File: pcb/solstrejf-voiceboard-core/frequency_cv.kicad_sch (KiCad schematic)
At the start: 23 parts, among them U5 LM324, U7 L78L12, U8 L79L12

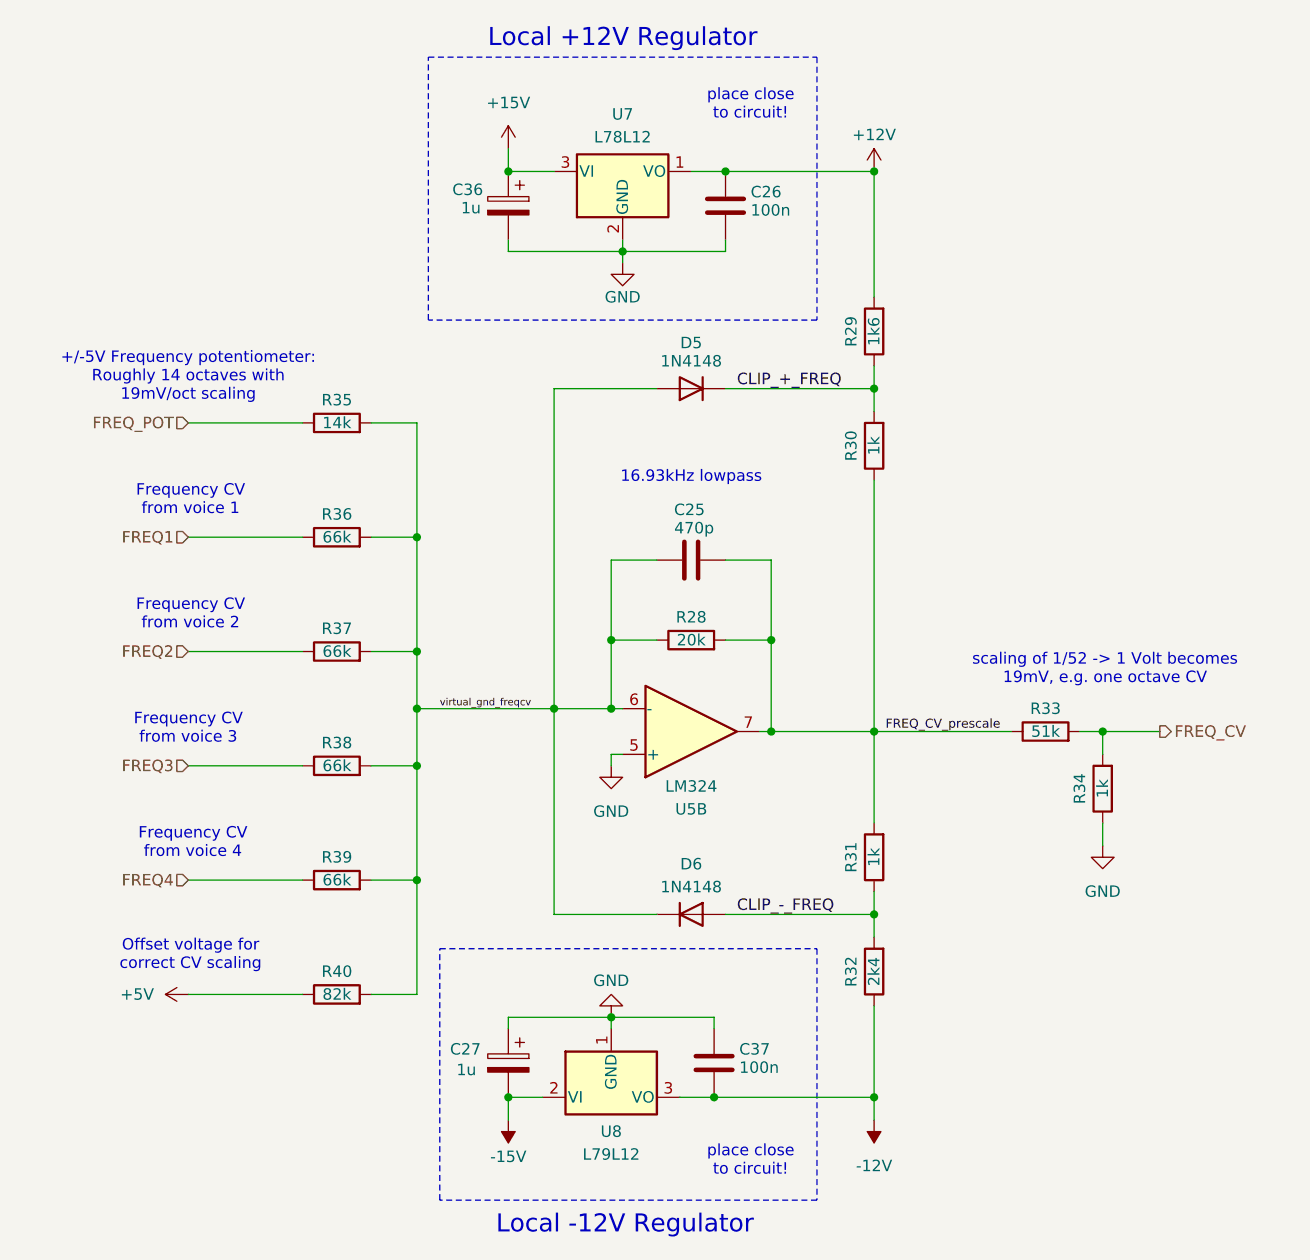
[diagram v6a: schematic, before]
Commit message: Updated values of electrolytic caps on voice board to match in the ibom.
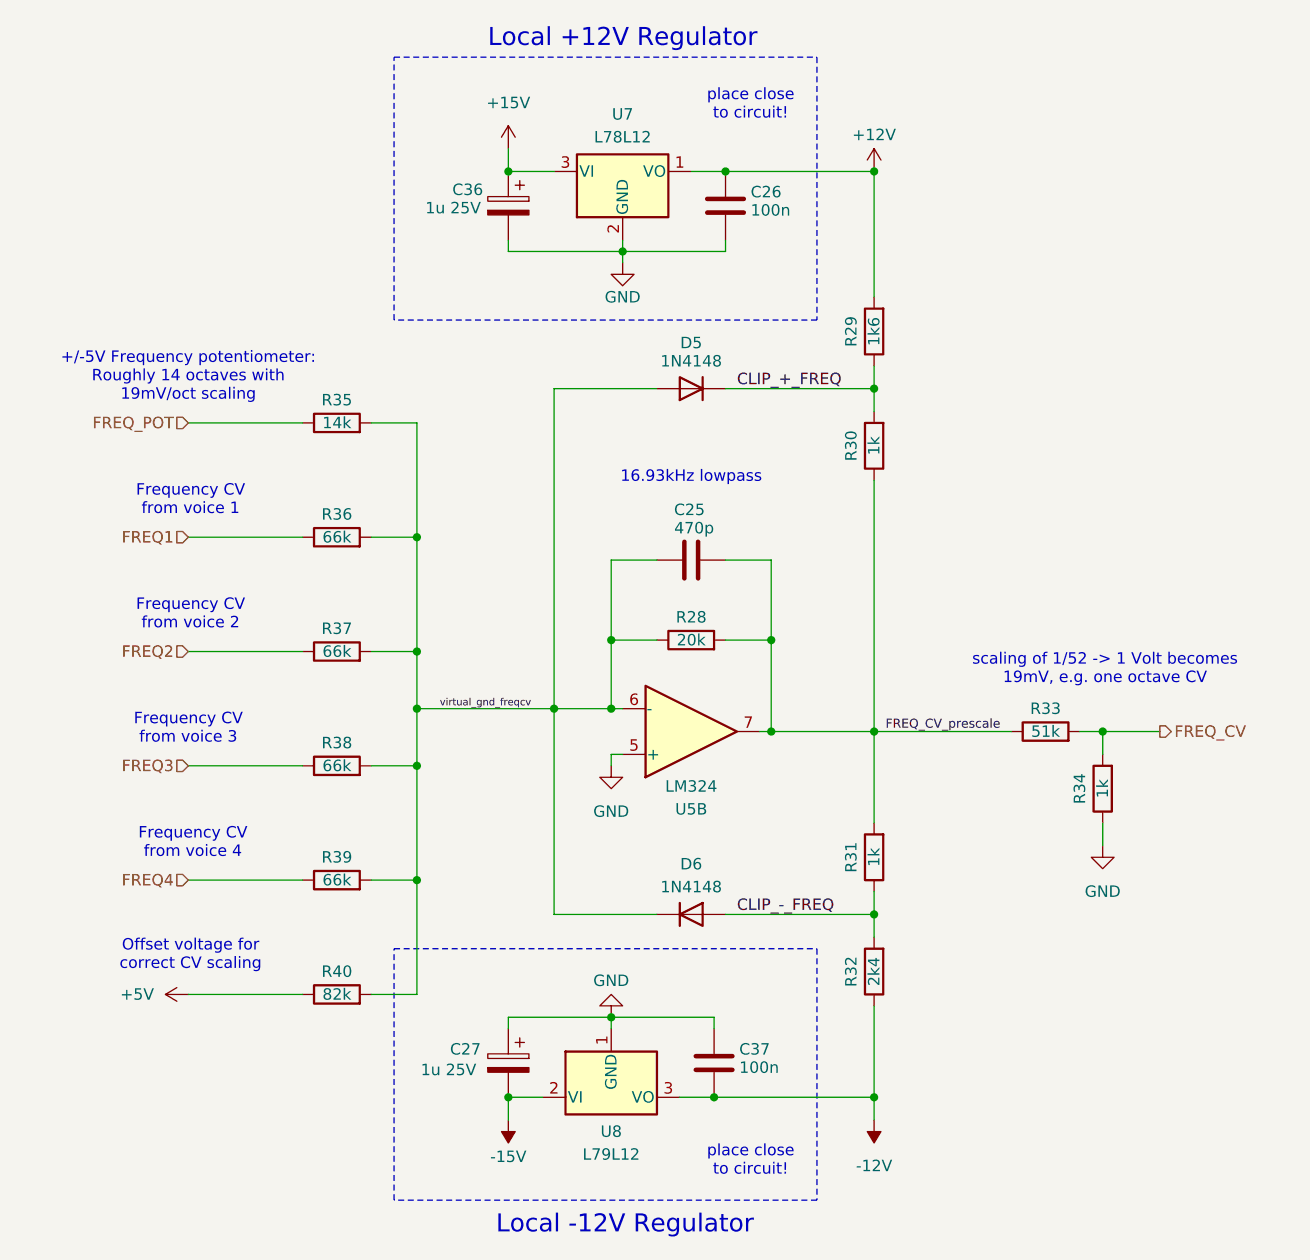
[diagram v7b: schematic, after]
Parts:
- C27, C36: value 1u -> 1u 25V
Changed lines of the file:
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@@
 	)
 	(rectangle
-		(start 102.87 26.67)
+		(start 99.06 26.67)
 		(end 146.05 55.88)
 		(stroke
@@
 	)
 	(rectangle
-		(start 104.14 125.73)
+		(start 99.06 125.73)
 		(end 146.05 153.67)
 		(stroke
@@
 			)
 		)
-		(property "Value" "1u"
+		(property "Value" "1u 25V"
 			(at 108.712 43.434 0)
 			(effects
@@
 			)
 		)
-		(property "Value" "1u"
+		(property "Value" "1u 25V"
 			(at 108.204 139.192 0)
 			(effects

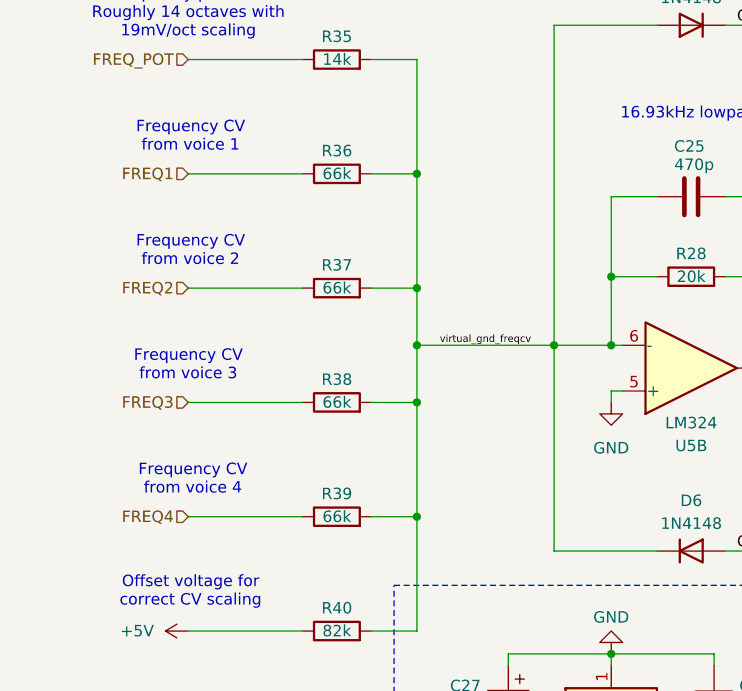
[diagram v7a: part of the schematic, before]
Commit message: Created rev1.1 of Solstref voice board. Updated value of some resistors (66k->68k). Exported new ibom and schematic.
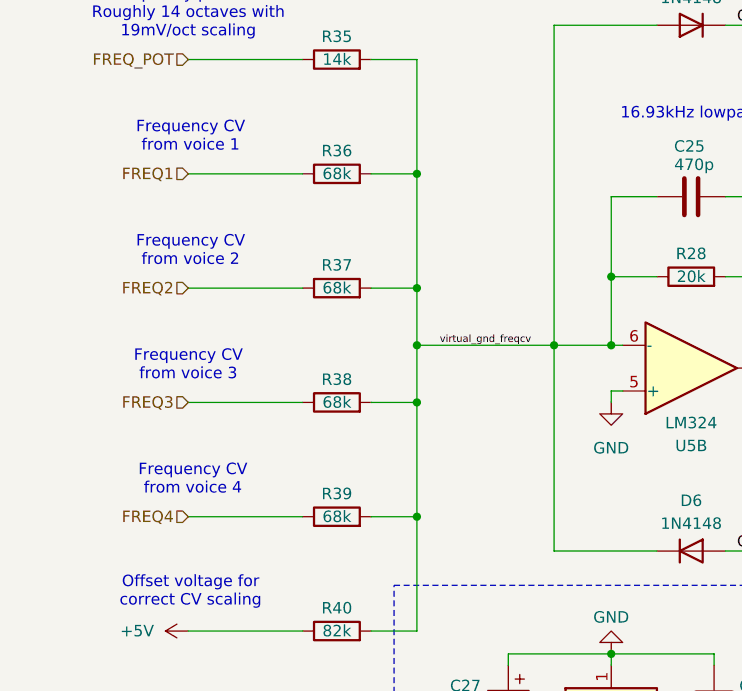
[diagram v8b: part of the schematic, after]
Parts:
- R36, R37, R38, R39: value 66k -> 68k
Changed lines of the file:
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@@
 (kicad_sch
-	(version 20231120)
+	(version 20250114)
 	(generator "eeschema")
-	(generator_version "8.0")
+	(generator_version "9.0")
 	(paper "A4")
 	(title_block
 		(title "Frequency Control Voltage Summing Amplifier")
-		(date "2024-10-28")
-		(rev "1.0")
+		(date "2025-03-01")
+		(rev "1.1")
+	)
+	(rectangle
+		(start 99.06 26.67)
+		(end 146.05 55.88)
+		(stroke
+			(width 0)
+			(type dash)
+		)
+		(fill
+			(type none)
+		)
+	)
+	(rectangle
+		(start 99.06 125.73)
+		(end 146.05 153.67)
+		(stroke
+			(width 0)
+			(type dash)
+		)
+		(fill
+			(type none)
+		)
+	)
+	(text "Offset voltage for\ncorrect CV scaling"
+		(exclude_from_sim no)
+		(at 76.454 128.27 0)
+		(effects
+			(font
+				(size 1.27 1.27)
+			)
+			(justify bottom)
+		)
+	)
+	(text "Local +12V Regulator"
+		(exclude_from_sim no)
+		(at 124.46 24.638 0)
+		(effects
+			(font
+				(size 2 2)
+			)
+		)
+	)
+	(text "16.93kHz lowpass"
+		(exclude_from_sim no)
+		(at 132.08 73.406 0)
+		(effects
+			(font
+				(size 1.27 1.27)
+			)
+		)
+	)
+	(text "Frequency CV \nfrom voice 3"
+		(exclude_from_sim no)
+		(at 76.2 103.124 0)
+		(effects
+			(font
+				(size 1.27 1.27)
+			)
+			(justify bottom)
+		)
+	)
+	(text "scaling of 1/52 -> 1 Volt becomes \n19mV, e.g. one octave CV"
+		(exclude_from_sim no)
+		(at 178.054 94.742 0)
+		(effects
+			(font
+				(size 1.27 1.27)
+			)
+		)
+	)
+	(text "Frequency CV \nfrom voice 2"
+		(exclude_from_sim no)
+		(at 76.454 90.424 0)
+		(effects
+			(font
+				(size 1.27 1.27)
+			)
+			(justify bottom)
+		)
+	)
+	(text "Frequency CV \nfrom voice 1"
+		(exclude_from_sim no)
+		(at 76.454 77.724 0)
+		(effects
+			(font
+				(size 1.27 1.27)
+			)
+			(justify bottom)
+		)
+	)
+	(text "place close \nto circuit!"
+		(exclude_from_sim no)
+		(at 138.684 151.13 0)
+		(effects
+			(font
+				(size 1.27 1.27)
+			)
+			(justify bottom)
+		)
+	)
+	(text "Frequency CV \nfrom voice 4"
+		(exclude_from_sim no)
+		(at 76.708 115.824 0)
+		(effects
+			(font
+				(size 1.27 1.27)
+			)
+			(justify bottom)
+		)
+	)
+	(text "Local -12V Regulator"
+		(exclude_from_sim no)
+		(at 124.714 156.464 0)
+		(effects
+			(font
+				(size 2 2)
+			)
+		)
+	)
+	(text "+/-5V Frequency potentiometer:\nRoughly 14 octaves with \n19mV/oct scaling"
+		(exclude_from_sim no)
+		(at 76.2 65.024 0)
+		(effects
+			(font
+				(size 1.27 1.27)
+			)
+			(justify bottom)
+		)
+	)
+	(text "place close \nto circuit!"
+		(exclude_from_sim no)
+		(at 138.684 33.782 0)
+		(effects
+			(font
+				(size 1.27 1.27)
+			)
+			(justify bottom)
+		)
 	)
 	(junction
@@
 		)
 	)
-	(rectangle
-		(start 99.06 26.67)
-		(end 146.05 55.88)
-		(stroke
-			(width 0)
-			(type dash)
-		)
-		(fill
-			(type none)
-		)
-	)
-	(rectangle
-		(start 99.06 125.73)
-		(end 146.05 153.67)
-		(stroke
-			(width 0)
-			(type dash)
-		)
-		(fill
-			(type none)
-		)
-	)
-	(text "Offset voltage for\ncorrect CV scaling"
-		(exclude_from_sim no)
-		(at 76.454 128.27 0)
+	(label "CLIP_+_FREQ"
+		(at 137.16 63.5 0)
 		(effects
 			(font
 				(size 1.27 1.27)
 			)
-			(justify bottom)
-		)
-	)
-	(text "Local +12V Regulator"
-		(exclude_from_sim no)
-		(at 124.46 24.638 0)
-		(effects
-			(font
-				(size 2 2)
-			)
-		)
-	)
-	(text "16.93kHz lowpass"
-		(exclude_from_sim no)
-		(at 132.08 73.406 0)
+			(justify left bottom)
+		)
+	)
+	(label "CLIP_-_FREQ"
+		(at 137.16 121.92 0)
 		(effects
 			(font
 				(size 1.27 1.27)
 			)
-		)
-	)
-	(text "Frequency CV \nfrom voice 3"
-		(exclude_from_sim no)
-		(at 76.2 103.124 0)
+			(justify left bottom)
+		)
+	)
+	(label "FREQ_CV_prescale"
+		(at 153.67 101.6 0)
+		(effects
+			(font
+				(size 1 1)
+			)
+			(justify left bottom)
+		)
+	)
+	(label "virtual_gnd_freqcv"
+		(at 104.14 99.06 0)
+		(effects
+			(font
+				(size 0.8 0.8)
+			)
+			(justify left bottom)
+		)
+	)
+	(hierarchical_label "FREQ3"
+		(shape input)
+		(at 76.2 105.41 180)
 		(effects
 			(font
 				(size 1.27 1.27)
 			)
-			(justify bottom)
-		)
-	)
-	(text "scaling of 1/52 -> 1 Volt becomes \n19mV, e.g. one octave CV"
-		(exclude_from_sim no)
-		(at 178.054 94.742 0)
+			(justify right)
+		)
+	)
+	(hierarchical_label "FREQ4"
+		(shape input)
+		(at 76.2 118.11 180)
 		(effects
 			(font
 				(size 1.27 1.27)
 			)
-		)
-	)
-	(text "Frequency CV \nfrom voice 2"
-		(exclude_from_sim no)
-		(at 76.454 90.424 0)
+			(justify right)
+		)
+	)
+	(hierarchical_label "FREQ_CV"
+		(shape output)
+		(at 184.15 101.6 0)
 		(effects
 			(font
 				(size 1.27 1.27)
 			)
-			(justify bottom)
-		)
-	)
-	(text "Frequency CV \nfrom voice 1"
-		(exclude_from_sim no)
-		(at 76.454 77.724 0)
+			(justify left)
+		)
+	)
+	(hierarchical_label "FREQ_POT"
+		(shape input)
+		(at 76.2 67.31 180)
 		(effects
 			(font
 				(size 1.27 1.27)
 			)
-			(justify bottom)
-		)
-	)
-	(text "place close \nto circuit!"
-		(exclude_from_sim no)
-		(at 138.684 151.13 0)
+			(justify right)
+		)
+	)
+	(hierarchical_label "FREQ2"
+		(shape input)
+		(at 76.2 92.71 180)
 		(effects
 			(font
 				(size 1.27 1.27)
 			)
-			(justify bottom)
-		)
-	)
-	(text "Frequency CV \nfrom voice 4"
-		(exclude_from_sim no)
-		(at 76.708 115.824 0)
-		(effects
-			(font
-				(size 1.27 1.27)
-			)
-			(justify bottom)
-		)
-	)
-	(text "Local -12V Regulator"
-		(exclude_from_sim no)
-		(at 124.714 156.464 0)
-		(effects
-			(font
-				(size 2 2)
-			)
-		)
-	)
-	(text "+/-5V Frequency potentiometer:\nRoughly 14 octaves with \n19mV/oct scaling"
-		(exclude_from_sim no)
-		(at 76.2 65.024 0)
-		(effects
-			(font
-				(size 1.27 1.27)
-			)
-			(justify bottom)
-		)
-	)
-	(text "place close \nto circuit!"
-		(exclude_from_sim no)
-		(at 138.684 33.782 0)
-		(effects
-			(font
-				(size 1.27 1.27)
-			)
-			(justify bottom)
-		)
-	)
-	(label "CLIP_+_FREQ"
-		(at 137.16 63.5 0)
-		(fields_autoplaced yes)
-		(effects
-			(font
-				(size 1.27 1.27)
-			)
-			(justify left bottom)
-		)
-	)
-	(label "CLIP_-_FREQ"
-		(at 137.16 121.92 0)
-		(fields_autoplaced yes)
-		(effects
-			(font
-				(size 1.27 1.27)
-			)
-			(justify left bottom)
-		)
-	)
-	(label "FREQ_CV_prescale"
-		(at 153.67 101.6 0)
-		(fields_autoplaced yes)
-		(effects
-			(font
-				(size 1 1)
-			)
-			(justify left bottom)
-		)
-	)
-	(label "virtual_gnd_freqcv"
-		(at 104.14 99.06 0)
-		(fields_autoplaced yes)
-		(effects
-			(font
-				(size 0.8 0.8)
-			)
-			(justify left bottom)
-		)
-	)
-	(hierarchical_label "FREQ3"
-		(shape input)
-		(at 76.2 105.41 180)
-		(fields_autoplaced yes)
-		(effects
-			(font
-				(size 1.27 1.27)
-			)
-			(justify right)
-		)
-	)
-	(hierarchical_label "FREQ4"
-		(shape input)
-		(at 76.2 118.11 180)
-		(fields_autoplaced yes)
-		(effects
-			(font
-				(size 1.27 1.27)
-			)
-			(justify right)
-		)
-	)
-	(hierarchical_label "FREQ_CV"
-		(shape output)
-		(at 184.15 101.6 0)
-		(fields_autoplaced yes)
-		(effects
-			(font
-				(size 1.27 1.27)
-			)
-			(justify left)
-		)
-	)
-	(hierarchical_label "FREQ_POT"
-		(shape input)
-		(at 76.2 67.31 180)
-		(fields_autoplaced yes)
-		(effects
-			(font
-				(size 1.27 1.27)
-			)
-			(justify right)
-		)
-	)
-	(hierarchical_label "FREQ2"
-		(shape input)
-		(at 76.2 92.71 180)
-		(fields_autoplaced yes)
-		(effects
-			(font
-				(size 1.27 1.27)
-			)
 			(justify right)
 		)
@@
 		(shape input)
 		(at 76.2 80.01 180)
-		(fields_autoplaced yes)
 		(effects
 			(font
@@
 			)
 		)
-		(property "Value" "66k"
+		(property "Value" "68k"
 			(at 92.71 105.41 90)
 			(effects
@@
 			)
 		)
-		(property "Value" "66k"
+		(property "Value" "68k"
 			(at 92.71 80.01 90)
 			(effects
@@
 			)
 		)
-		(property "Value" "66k"
+		(property "Value" "68k"
 			(at 92.71 118.11 90)
 			(effects
@@
 			)
 		)
-		(property "Value" "66k"
+		(property "Value" "68k"
 			(at 92.71 92.71 90)
 			(effects
